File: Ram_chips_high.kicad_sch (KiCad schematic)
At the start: 10 parts, among them U25 MM5280, U26 MM5280, U27 MM5280, U28 MM5280, U40 MM5280, U41 MM5280, U42 MM5280, U43 MM5280, U6 74LS04, U7 74LS173

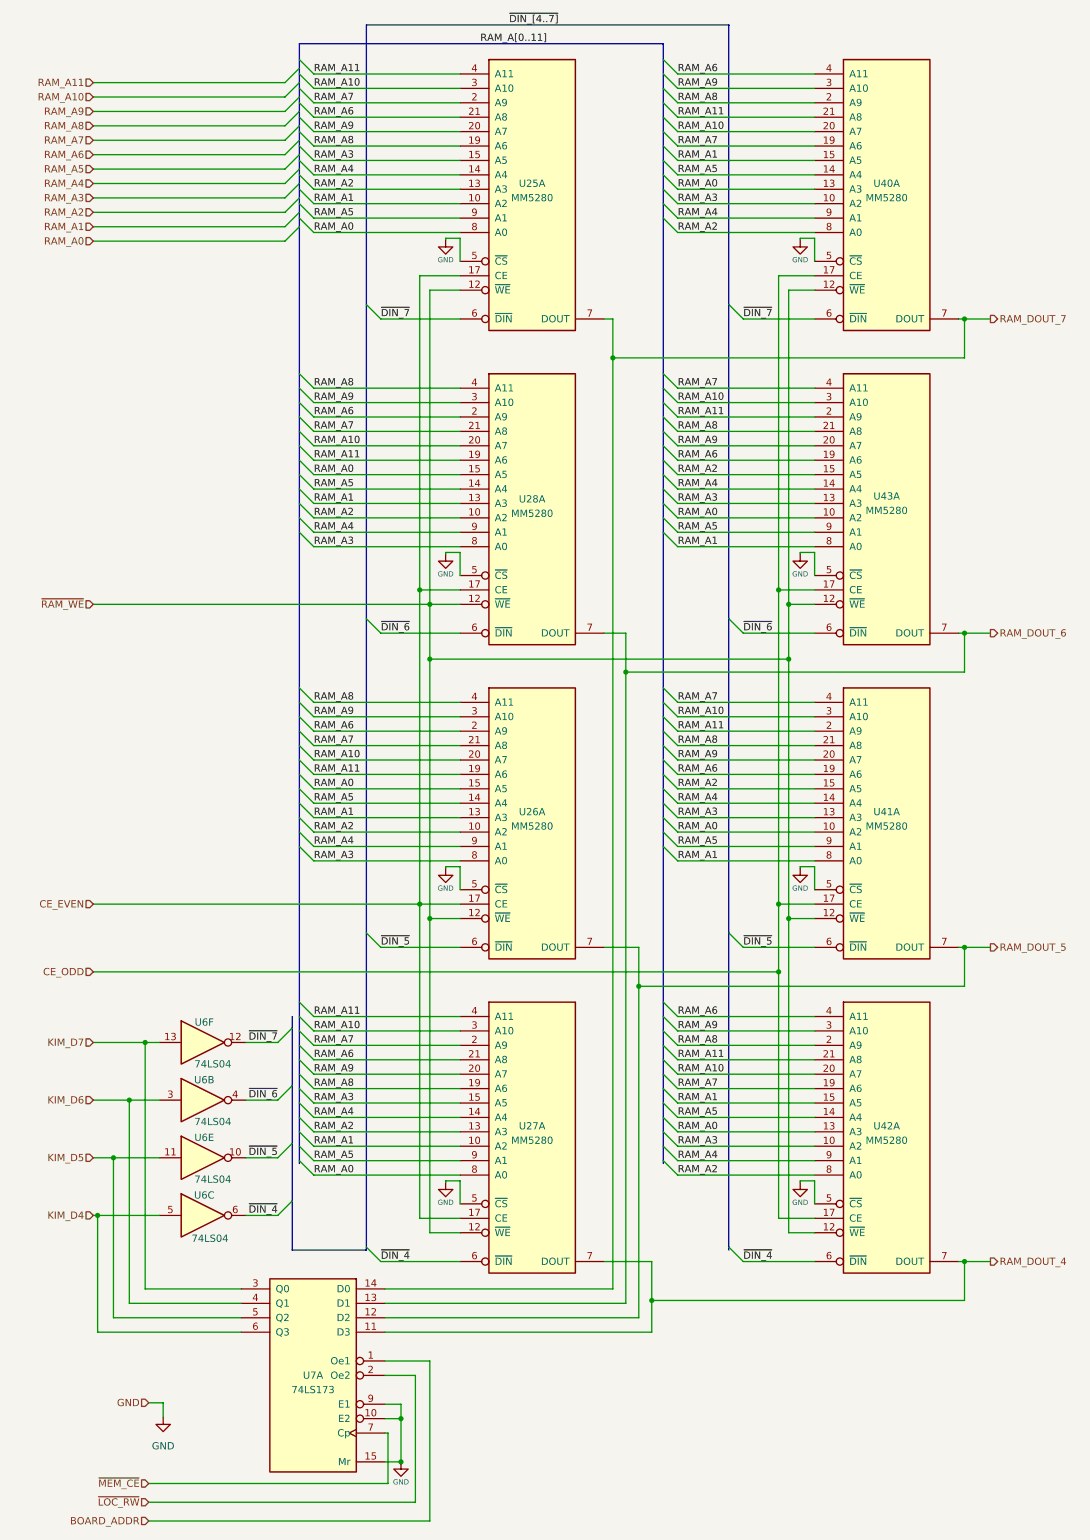
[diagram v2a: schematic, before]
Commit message: Swap high and low RAM nibbles
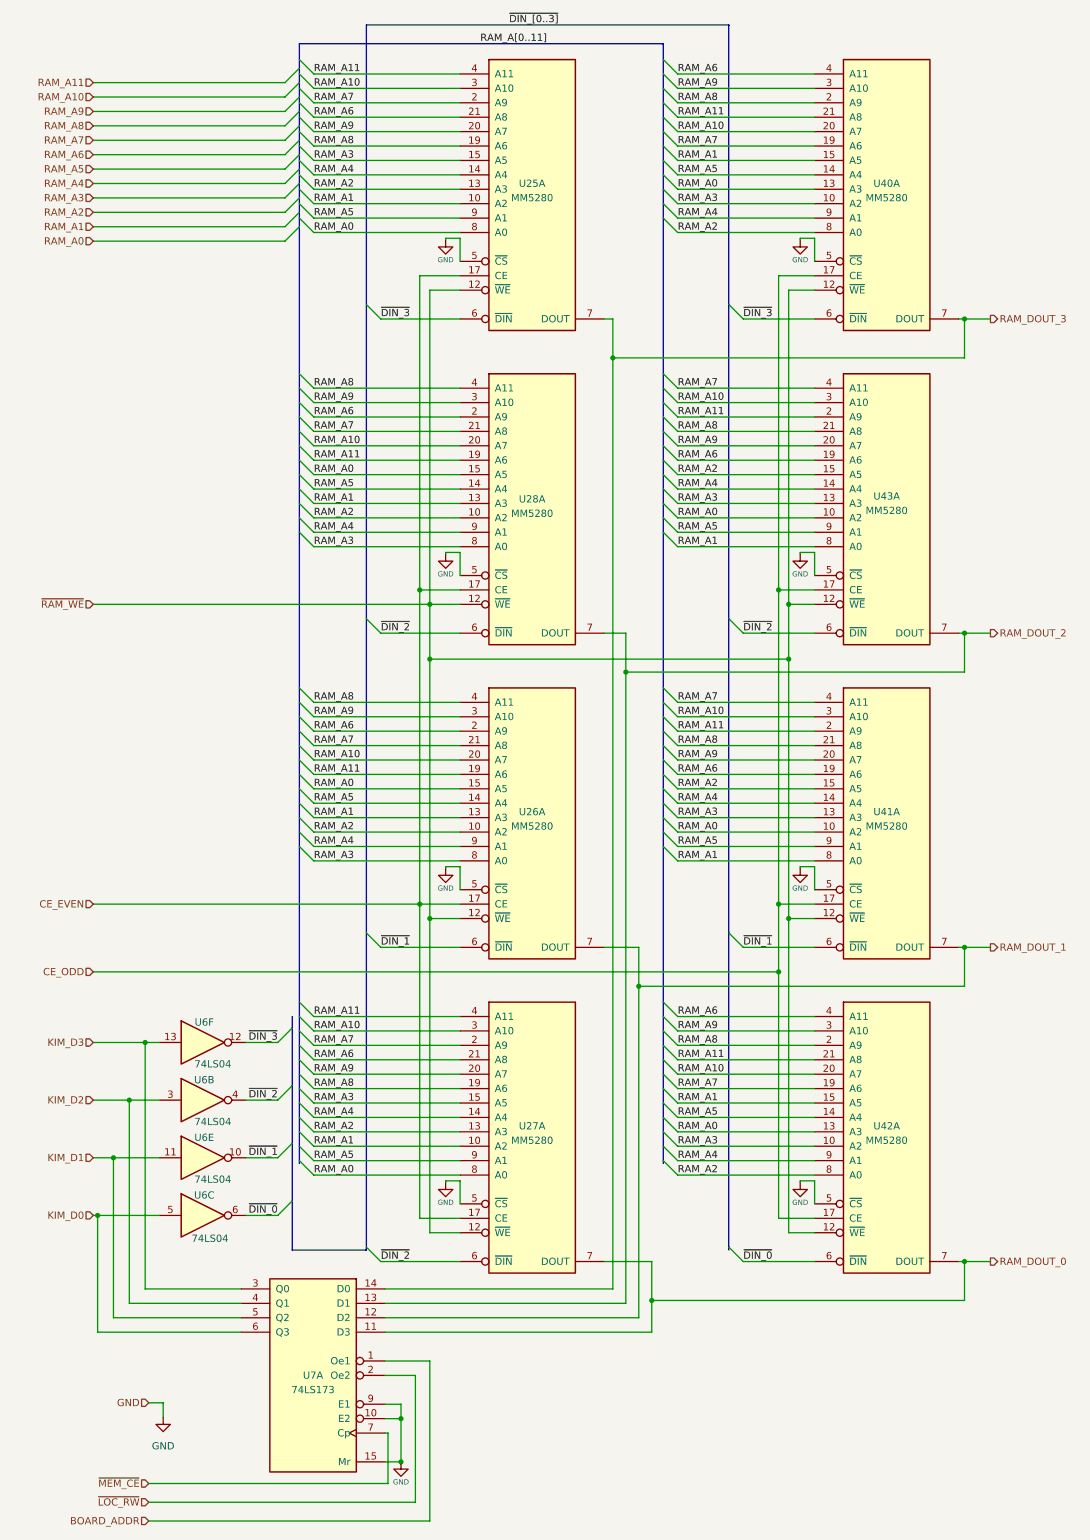
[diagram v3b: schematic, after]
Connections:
- net KIM_D4 renamed KIM_D0
- net KIM_D5 renamed KIM_D1
- net KIM_D6 renamed KIM_D2
- net KIM_D7 renamed KIM_D3
- net RAM_DOUT_4 renamed RAM_DOUT_0
- net RAM_DOUT_5 renamed RAM_DOUT_1
- net RAM_DOUT_6 renamed RAM_DOUT_2
- net RAM_DOUT_7 renamed RAM_DOUT_3
- net ~{DIN_4} renamed ~{DIN_0}
- net ~{DIN_0}: no longer U27.6 (~{DIN})
- net ~{DIN_5} renamed ~{DIN_1}
- net ~{DIN_6} renamed ~{DIN_2}
- net ~{DIN_2}: now also U27.6 (~{DIN})
- net ~{DIN_7} renamed ~{DIN_3}
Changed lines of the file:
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@@
     (effects (font (size 1.27 1.27)) (justify left bottom))
   )
-  (label "~{DIN_6}" (at 138.557 122.936 0) (fields_autoplaced)
+  (label "~{DIN_2}" (at 138.557 122.936 0) (fields_autoplaced)
     (effects (font (size 1.27 1.27)) (justify left bottom))
   )
@@
     (effects (font (size 1.27 1.27)) (justify left bottom))
   )
-  (label "~{DIN_7}" (at 56.515 195.072 180) (fields_autoplaced)
+  (label "~{DIN_3}" (at 56.515 195.072 180) (fields_autoplaced)
     (effects (font (size 1.27 1.27)) (justify right bottom))
   )
@@
     (effects (font (size 1.27 1.27)) (justify left bottom))
   )
-  (label "~{DIN_6}" (at 74.676 122.936 0) (fields_autoplaced)
+  (label "~{DIN_2}" (at 74.676 122.936 0) (fields_autoplaced)
     (effects (font (size 1.27 1.27)) (justify left bottom))
   )
@@
     (effects (font (size 1.27 1.27)) (justify left bottom))
   )
-  (label "~{DIN_4}" (at 138.557 233.68 0) (fields_autoplaced)
+  (label "~{DIN_0}" (at 138.557 233.68 0) (fields_autoplaced)
     (effects (font (size 1.27 1.27)) (justify left bottom))
   )
@@
     (effects (font (size 1.27 1.27)) (justify left bottom))
   )
-  (label "~{DIN_4}" (at 74.676 233.68 0) (fields_autoplaced)
+  (label "~{DIN_2}" (at 74.676 233.68 0) (fields_autoplaced)
     (effects (font (size 1.27 1.27)) (justify left bottom))
   )
@@
     (effects (font (size 1.27 1.27)) (justify left bottom))
   )
-  (label "~{DIN_4}" (at 56.515 225.552 180) (fields_autoplaced)
+  (label "~{DIN_0}" (at 56.515 225.552 180) (fields_autoplaced)
     (effects (font (size 1.27 1.27)) (justify right bottom))
   )
@@
     (effects (font (size 1.27 1.27)) (justify left bottom))
   )
-  (label "~{DIN_5}" (at 138.557 178.308 0) (fields_autoplaced)
+  (label "~{DIN_1}" (at 138.557 178.308 0) (fields_autoplaced)
     (effects (font (size 1.27 1.27)) (justify left bottom))
   )
@@
     (effects (font (size 1.27 1.27)) (justify left bottom))
   )
-  (label "~{DIN_[4..7]}" (at 97.282 15.748 0) (fields_autoplaced)
+  (label "~{DIN_[0..3]}" (at 97.282 15.748 0) (fields_autoplaced)
     (effects (font (size 1.27 1.27)) (justify left bottom))
   )
@@
     (effects (font (size 1.27 1.27)) (justify left bottom))
   )
-  (label "~{DIN_7}" (at 138.557 67.564 0) (fields_autoplaced)
+  (label "~{DIN_3}" (at 138.557 67.564 0) (fields_autoplaced)
     (effects (font (size 1.27 1.27)) (justify left bottom))
   )
@@
     (effects (font (size 1.27 1.27)) (justify left bottom))
   )
-  (label "~{DIN_6}" (at 56.515 205.232 180) (fields_autoplaced)
+  (label "~{DIN_2}" (at 56.515 205.232 180) (fields_autoplaced)
     (effects (font (size 1.27 1.27)) (justify right bottom))
   )
@@
     (effects (font (size 1.27 1.27)) (justify left bottom))
   )
-  (label "~{DIN_7}" (at 74.676 67.564 0) (fields_autoplaced)
+  (label "~{DIN_3}" (at 74.676 67.564 0) (fields_autoplaced)
     (effects (font (size 1.27 1.27)) (justify left bottom))
   )
@@
     (effects (font (size 1.27 1.27)) (justify left bottom))
   )
-  (label "~{DIN_5}" (at 56.515 215.392 180) (fields_autoplaced)
+  (label "~{DIN_1}" (at 56.515 215.392 180) (fields_autoplaced)
     (effects (font (size 1.27 1.27)) (justify right bottom))
   )
@@
     (effects (font (size 1.27 1.27)) (justify left bottom))
   )
-  (label "~{DIN_5}" (at 74.676 178.308 0) (fields_autoplaced)
+  (label "~{DIN_1}" (at 74.676 178.308 0) (fields_autoplaced)
     (effects (font (size 1.27 1.27)) (justify left bottom))
   )
@@
     (effects (font (size 1.27 1.27)) (justify right))
   )
-  (hierarchical_label "KIM_D4" (shape input) (at 24.003 225.552 180) (fields_autoplaced)
+  (hierarchical_label "KIM_D0" (shape input) (at 24.003 225.552 180) (fields_autoplaced)
     (effects (font (size 1.27 1.27)) (justify right))
   )
@@
     (effects (font (size 1.27 1.27)) (justify right))
   )
-  (hierarchical_label "KIM_D7" (shape input) (at 24.003 195.072 180) (fields_autoplaced)
+  (hierarchical_label "KIM_D3" (shape input) (at 24.003 195.072 180) (fields_autoplaced)
     (effects (font (size 1.27 1.27)) (justify right))
   )
@@
     (effects (font (size 1.27 1.27)) (justify right))
   )
-  (hierarchical_label "RAM_DOUT_5" (shape output) (at 182.118 178.308 0) (fields_autoplaced)
+  (hierarchical_label "RAM_DOUT_1" (shape output) (at 182.118 178.308 0) (fields_autoplaced)
     (effects (font (size 1.27 1.27)) (justify left))
   )
@@
     (effects (font (size 1.27 1.27)) (justify right))
   )
-  (hierarchical_label "RAM_DOUT_7" (shape output) (at 182.118 67.564 0) (fields_autoplaced)
+  (hierarchical_label "RAM_DOUT_3" (shape output) (at 182.118 67.564 0) (fields_autoplaced)
     (effects (font (size 1.27 1.27)) (justify left))
   )
@@
     (effects (font (size 1.27 1.27)) (justify right))
   )
-  (hierarchical_label "KIM_D6" (shape input) (at 24.003 205.232 180) (fields_autoplaced)
-    (effects (font (size 1.27 1.27)) (justify right))
-  )
-  (hierarchical_label "RAM_DOUT_4" (shape output) (at 182.118 233.68 0) (fields_autoplaced)
+  (hierarchical_label "KIM_D2" (shape input) (at 24.003 205.232 180) (fields_autoplaced)
+    (effects (font (size 1.27 1.27)) (justify right))
+  )
+  (hierarchical_label "RAM_DOUT_0" (shape output) (at 182.118 233.68 0) (fields_autoplaced)
     (effects (font (size 1.27 1.27)) (justify left))
   )
@@
     (effects (font (size 1.27 1.27)) (justify right))
   )
-  (hierarchical_label "KIM_D5" (shape input) (at 24.003 215.392 180) (fields_autoplaced)
+  (hierarchical_label "KIM_D1" (shape input) (at 24.003 215.392 180) (fields_autoplaced)
     (effects (font (size 1.27 1.27)) (justify right))
   )
@@
     (effects (font (size 1.27 1.27)) (justify right))
   )
-  (hierarchical_label "RAM_DOUT_6" (shape output) (at 182.118 122.936 0) (fields_autoplaced)
+  (hierarchical_label "RAM_DOUT_2" (shape output) (at 182.118 122.936 0) (fields_autoplaced)
     (effects (font (size 1.27 1.27)) (justify left))
   )

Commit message: Routing completed
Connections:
- net RAM_DOUT_0: now also U27.16 (N/C), U42.16 (N/C)
- net RAM_DOUT_1: now also U26.16 (N/C), U41.16 (N/C)
- net RAM_DOUT_2: now also U28.16 (N/C), U43.16 (N/C)
- net RAM_DOUT_3: now also U25.16 (N/C), U40.16 (N/C)
- net ~{DIN_0}: now also U27.6 (~{DIN})
- net ~{DIN_2}: no longer U27.6 (~{DIN})
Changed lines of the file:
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@@
   (junction (at 177.546 122.936) (diameter 0) (color 0 0 0 0)
   )
+  (junction (at 122.428 233.68) (diameter 0) (color 0 0 0 0)
+  )
   (junction (at 177.546 67.564) (diameter 0) (color 0 0 0 0)
   )
@@
   (junction (at 83.312 117.856) (diameter 0) (color 0 0 0 0)
   )
+  (junction (at 120.142 178.308) (diameter 0) (color 0 0 0 0)
+  )
   (junction (at 117.856 129.794) (diameter 0) (color 0 0 0 0)
   )
+  (junction (at 117.856 122.936) (diameter 0) (color 0 0 0 0)
+  )
+  (junction (at 115.57 67.564) (diameter 0) (color 0 0 0 0)
+  )
   (junction (at 144.78 170.688) (diameter 0) (color 0 0 0 0)
   )
@@
     (stroke (width 0) (type default))
   )
+  (wire (pts (xy 122.428 228.6) (xy 122.428 233.68))
+    (stroke (width 0) (type default))
+  )
   (wire (pts (xy 83.312 173.228) (xy 88.646 173.228))
     (stroke (width 0) (type default))
@@
     (stroke (width 0) (type default))
   )
+  (wire (pts (xy 176.53 117.856) (xy 177.546 117.856))
+    (stroke (width 0) (type default))
+  )
   (wire (pts (xy 148.59 164.338) (xy 148.59 164.084))
     (stroke (width 0) (type default))
@@
     (stroke (width 0) (type default))
   )
+  (wire (pts (xy 114.046 117.856) (xy 117.856 117.856))
+    (stroke (width 0) (type default))
+  )
   (wire (pts (xy 127 97.536) (xy 151.13 97.536))
     (stroke (width 0) (type default))
@@
     (stroke (width 0) (type default))
   )
+  (wire (pts (xy 176.53 228.6) (xy 177.546 228.6))
+    (stroke (width 0) (type default))
+  )
   (bus (pts (xy 72.136 65.024) (xy 72.136 120.396))
     (stroke (width 0) (type default))
@@
     (stroke (width 0) (type default))
   )
+  (wire (pts (xy 177.546 62.484) (xy 177.546 67.564))
+    (stroke (width 0) (type default))
+  )
   (wire (pts (xy 74.676 67.564) (xy 88.646 67.564))
     (stroke (width 0) (type default))
@@
     (stroke (width 0) (type default))
   )
+  (wire (pts (xy 115.57 62.484) (xy 115.57 67.564))
+    (stroke (width 0) (type default))
+  )
   (bus (pts (xy 124.46 215.9) (xy 124.46 216.408))
     (stroke (width 0) (type default))
@@
     (stroke (width 0) (type default))
   )
+  (wire (pts (xy 120.142 173.228) (xy 120.142 178.308))
+    (stroke (width 0) (type default))
+  )
   (bus (pts (xy 60.325 44.704) (xy 60.325 46.228))
     (stroke (width 0) (type default))
@@
     (stroke (width 0) (type default))
   )
+  (wire (pts (xy 177.546 173.228) (xy 177.546 178.308))
+    (stroke (width 0) (type default))
+  )
   (wire (pts (xy 62.865 140.208) (xy 88.646 140.208))
     (stroke (width 0) (type default))
@@
     (stroke (width 0) (type default))
   )
+  (wire (pts (xy 114.046 228.6) (xy 122.428 228.6))
+    (stroke (width 0) (type default))
+  )
   (bus (pts (xy 124.46 29.464) (xy 124.46 26.924))
     (stroke (width 0) (type default))
@@
     (stroke (width 0) (type default))
   )
+  (wire (pts (xy 117.856 117.856) (xy 117.856 122.936))
+    (stroke (width 0) (type default))
+  )
   (wire (pts (xy 127 107.696) (xy 151.13 107.696))
     (stroke (width 0) (type default))
@@
     (stroke (width 0) (type default))
   )
+  (wire (pts (xy 114.046 62.484) (xy 115.57 62.484))
+    (stroke (width 0) (type default))
+  )
   (wire (pts (xy 62.865 102.616) (xy 88.646 102.616))
     (stroke (width 0) (type default))
@@
     (stroke (width 0) (type default))
   )
+  (wire (pts (xy 176.53 173.228) (xy 177.546 173.228))
+    (stroke (width 0) (type default))
+  )
   (bus (pts (xy 60.325 200.66) (xy 60.325 203.2))
     (stroke (width 0) (type default))
@@
     (stroke (width 0) (type default))
   )
+  (wire (pts (xy 177.546 117.856) (xy 177.546 122.936))
+    (stroke (width 0) (type default))
+  )
+  (wire (pts (xy 177.546 228.6) (xy 177.546 233.68))
+    (stroke (width 0) (type default))
+  )
   (bus (pts (xy 60.325 105.156) (xy 60.325 132.588))
     (stroke (width 0) (type default))
@@
     (stroke (width 0) (type default))
   )
+  (wire (pts (xy 114.046 173.228) (xy 120.142 173.228))
+    (stroke (width 0) (type default))
+  )
   (wire (pts (xy 33.782 272.796) (xy 75.946 272.796))
     (stroke (width 0) (type default))
@@
   )
   (bus (pts (xy 124.46 152.908) (xy 124.46 155.448))
+    (stroke (width 0) (type default))
+  )
+  (wire (pts (xy 176.53 62.484) (xy 177.546 62.484))
     (stroke (width 0) (type default))
   )
@@
     (effects (font (size 1.27 1.27)) (justify left bottom))
   )
-  (label "~{DIN_2}" (at 74.676 233.68 0) (fields_autoplaced)
-    (effects (font (size 1.27 1.27)) (justify left bottom))
-  )
+  (label "~{DIN_0}" (at 74.676 233.68 0) (fields_autoplaced)
+    (effects (font (size 1.27 1.27)) (justify left bottom))
+  )
